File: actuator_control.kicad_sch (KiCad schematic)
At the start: 5 parts, among them J7 Conn_01x02, Q2 BSS138

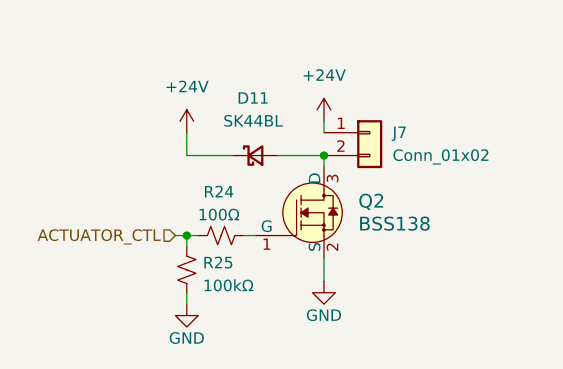
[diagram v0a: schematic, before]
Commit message: add heater connectors
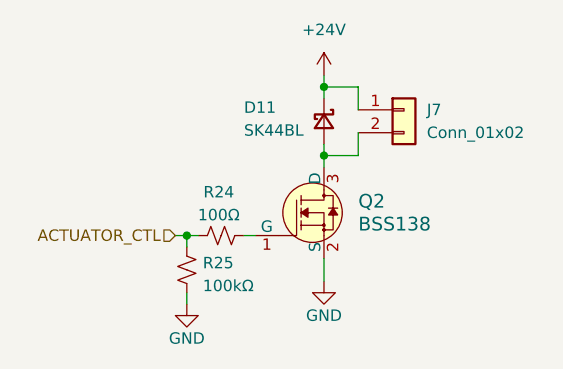
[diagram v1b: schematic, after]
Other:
- moved on the sheet: D11, J7
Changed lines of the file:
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@@
 		(color 0 0 0 0)
 	)
+	(junction
+		(at 110.49 50.8)
+		(diameter 0)
+		(color 0 0 0 0)
+	)
 	(wire
 		(pts
@@
 	(wire
 		(pts
-			(xy 95.25 55.88) (xy 95.25 58.42)
-		)
-		(stroke
-			(width 0)
-			(type default)
-		)
-	)
-	(wire
-		(pts
-			(xy 110.49 54.61) (xy 110.49 55.88)
+			(xy 110.49 57.15) (xy 110.49 58.42)
 		)
 		(stroke
@@
 	(wire
 		(pts
+			(xy 114.3 53.34) (xy 114.3 50.8)
+		)
+		(stroke
+			(width 0)
+			(type default)
+		)
+	)
+	(wire
+		(pts
+			(xy 110.49 50.8) (xy 114.3 50.8)
+		)
+		(stroke
+			(width 0)
+			(type default)
+		)
+	)
+	(wire
+		(pts
 			(xy 110.49 69.85) (xy 110.49 72.39)
 		)
@@
 	(wire
 		(pts
+			(xy 114.3 55.88) (xy 114.3 58.42)
+		)
+		(stroke
+			(width 0)
+			(type default)
+		)
+	)
+	(wire
+		(pts
+			(xy 110.49 50.8) (xy 110.49 52.07)
+		)
+		(stroke
+			(width 0)
+			(type default)
+		)
+	)
+	(wire
+		(pts
+			(xy 114.3 58.42) (xy 110.49 58.42)
+		)
+		(stroke
+			(width 0)
+			(type default)
+		)
+	)
+	(wire
+		(pts
 			(xy 95.25 67.31) (xy 95.25 68.58)
 		)
@@
 	(wire
 		(pts
-			(xy 100.33 58.42) (xy 95.25 58.42)
-		)
-		(stroke
-			(width 0)
-			(type default)
-		)
-	)
-	(wire
-		(pts
-			(xy 105.41 58.42) (xy 110.49 58.42)
+			(xy 110.49 49.53) (xy 110.49 50.8)
 		)
 		(stroke
@@
 	(symbol
 		(lib_id "Device:D_Schottky_Small")
-		(at 102.87 58.42 0)
+		(at 110.49 54.61 270)
 		(unit 1)
 		(body_style 1)
@@
 		(in_pos_files no)
 		(dnp no)
-		(fields_autoplaced yes)
 		(property "Reference" "D11"
-			(at 102.616 52.07 0)
-			(show_name no)
-			(do_not_autoplace no)
-			(effects
-				(font
-					(size 1.27 1.27)
-				)
+			(at 101.6 53.086 90)
+			(show_name no)
+			(do_not_autoplace no)
+			(effects
+				(font
+					(size 1.27 1.27)
+				)
+				(justify left)
 			)
 		)
 		(property "Value" "SK44BL"
-			(at 102.616 54.61 0)
-			(show_name no)
-			(do_not_autoplace no)
-			(effects
-				(font
-					(size 1.27 1.27)
-				)
+			(at 101.6 55.626 90)
+			(show_name no)
+			(do_not_autoplace no)
+			(effects
+				(font
+					(size 1.27 1.27)
+				)
+				(justify left)
 			)
 		)
 		(property "Footprint" "Diode_SMD:D_SMB"
-			(at 102.87 58.42 90)
+			(at 110.49 54.61 90)
 			(hide yes)
 			(show_name no)
@@
 		)
 		(property "Datasheet" ""
-			(at 102.87 58.42 90)
+			(at 110.49 54.61 90)
 			(hide yes)
 			(show_name no)
@@
 		)
 		(property "Description" "Schottky diode, small symbol"
-			(at 102.87 58.42 0)
+			(at 110.49 54.61 0)
 			(hide yes)
 			(show_name no)
@@
 		)
 		(property "LCSC" "C151740"
-			(at 102.87 58.42 0)
+			(at 110.49 54.61 0)
 			(hide yes)
 			(show_name no)
@@
 	)
 	(symbol
-		(lib_id "power:+24V")
-		(at 95.25 55.88 0)
-		(unit 1)
-		(body_style 1)
-		(exclude_from_sim no)
-		(in_bom yes)
-		(on_board yes)
-		(in_pos_files yes)
-		(dnp no)
-		(fields_autoplaced yes)
-		(property "Reference" "#PWR071"
-			(at 95.25 59.69 0)
-			(hide yes)
-			(show_name no)
-			(do_not_autoplace no)
-			(effects
-				(font
-					(size 1.27 1.27)
-				)
-			)
-		)
-		(property "Value" "+24V"
-			(at 95.25 50.8 0)
-			(show_name no)
-			(do_not_autoplace no)
-			(effects
-				(font
-					(size 1.27 1.27)
-				)
-			)
-		)
-		(property "Footprint" ""
-			(at 95.25 55.88 0)
-			(hide yes)
-			(show_name no)
-			(do_not_autoplace no)
-			(effects
-				(font
-					(size 1.27 1.27)
-				)
-			)
-		)
-		(property "Datasheet" ""
-			(at 95.25 55.88 0)
-			(hide yes)
-			(show_name no)
-			(do_not_autoplace no)
-			(effects
-				(font
-					(size 1.27 1.27)
-				)
-			)
-		)
-		(property "Description" "Power symbol creates a global label with name \"+24V\""
-			(at 95.25 55.88 0)
-			(hide yes)
-			(show_name no)
-			(do_not_autoplace no)
-			(effects
-				(font
-					(size 1.27 1.27)
-				)
-			)
-		)
-		(pin "1"
-		)
-		(instances
-			(project "gse_control_node"
-				(path "/24817451-dfe0-4b9a-9d93-7304529c9d58/3ca34fcb-848a-442f-9018-9caf10b9e369"
-					(reference "#PWR079")
-					(unit 1)
-				)
-				(path "/24817451-dfe0-4b9a-9d93-7304529c9d58/93ade7e9-ef13-409d-a430-89296b231c7f"
-					(reference "#PWR075")
-					(unit 1)
-				)
-				(path "/24817451-dfe0-4b9a-9d93-7304529c9d58/c4e569fb-235e-4777-b718-8e9c9d97ed61"
-					(reference "#PWR083")
-					(unit 1)
-				)
-				(path "/24817451-dfe0-4b9a-9d93-7304529c9d58/fe2b7ba1-9565-4f89-9bf9-1d97bef2da17"
-					(reference "#PWR071")
-					(unit 1)
-				)
-			)
-		)
-	)
-	(symbol
 		(lib_id "power:GND")
 		(at 95.25 74.93 0)
@@
 	(symbol
 		(lib_id "power:+24V")
-		(at 110.49 54.61 0)
+		(at 110.49 49.53 0)
 		(unit 1)
 		(body_style 1)
@@
 		(fields_autoplaced yes)
 		(property "Reference" "#PWR073"
-			(at 110.49 58.42 0)
+			(at 110.49 53.34 0)
 			(hide yes)
 			(show_name no)
@@
 		)
 		(property "Value" "+24V"
+			(at 110.49 44.45 0)
+			(show_name no)
+			(do_not_autoplace no)
+			(effects
+				(font
+					(size 1.27 1.27)
+				)
+			)
+		)
+		(property "Footprint" ""
 			(at 110.49 49.53 0)
-			(show_name no)
-			(do_not_autoplace no)
-			(effects
-				(font
-					(size 1.27 1.27)
-				)
-			)
-		)
-		(property "Footprint" ""
-			(at 110.49 54.61 0)
 			(hide yes)
 			(show_name no)
@@
 		)
 		(property "Datasheet" ""
-			(at 110.49 54.61 0)
+			(at 110.49 49.53 0)
 			(hide yes)
 			(show_name no)
@@
 		)
 		(property "Description" "Power symbol creates a global label with name \"+24V\""
-			(at 110.49 54.61 0)
+			(at 110.49 49.53 0)
 			(hide yes)
 			(show_name no)
@@
 	(symbol
 		(lib_id "Connector_Generic:Conn_01x02")
-		(at 115.57 55.88 0)
+		(at 119.38 53.34 0)
 		(unit 1)
 		(body_style 1)
@@
 		(fields_autoplaced yes)
 		(property "Reference" "J7"
-			(at 118.11 55.8799 0)
+			(at 121.92 53.3399 0)
 			(show_name no)
 			(do_not_autoplace no)
@@
 		)
 		(property "Value" "Conn_01x02"
-			(at 118.11 58.4199 0)
+			(at 121.92 55.8799 0)
 			(show_name no)
 			(do_not_autoplace no)
@@
 		)
 		(property "Footprint" "Connector_Molex:Molex_Micro-Fit_3.0_43650-0215_1x02_P3.00mm_Vertical"
-			(at 115.57 55.88 0)
+			(at 119.38 53.34 0)
 			(hide yes)
 			(show_name no)
@@
 		)
 		(property "Datasheet" ""
-			(at 115.57 55.88 0)
+			(at 119.38 53.34 0)
 			(hide yes)
 			(show_name no)
@@
 		)
 		(property "Description" "Generic connector, single row, 01x02, script generated (kicad-library-utils/schlib/autogen/connector/)"
-			(at 115.57 55.88 0)
+			(at 119.38 53.34 0)
 			(hide yes)
 			(show_name no)
@@
 		)
 		(property "LCSC" "N/A"
-			(at 115.57 55.88 0)
-			(hide yes)
-			(show_name no)
+			(at 119.38 53.34 0)
+			(hide yes)
+			(show_name no)
